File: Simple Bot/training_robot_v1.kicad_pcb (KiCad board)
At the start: 2 copper layers, 14 parts, among them J1 Conn_01x08_Socket, J2 Conn_01x04_Socket, J3 Conn_01x04_Socket, M1 Motor_DC, M2 Motor_DC, M3 Motor_DC, M4 Motor_DC, SW1 SW_SPDT_312

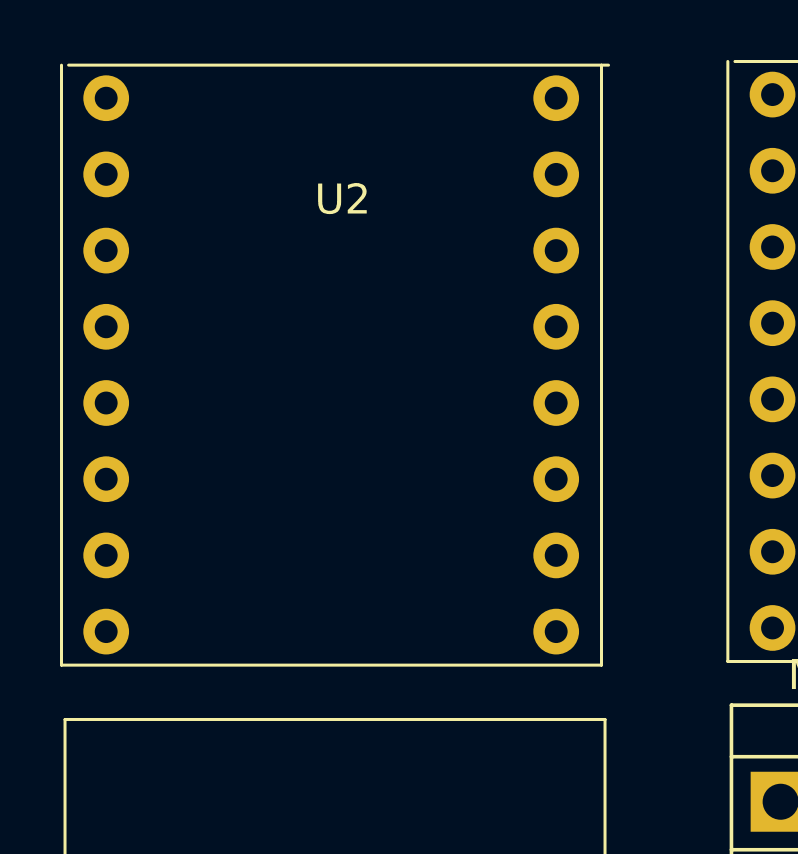
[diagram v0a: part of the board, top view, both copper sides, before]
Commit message: Removed schematic details
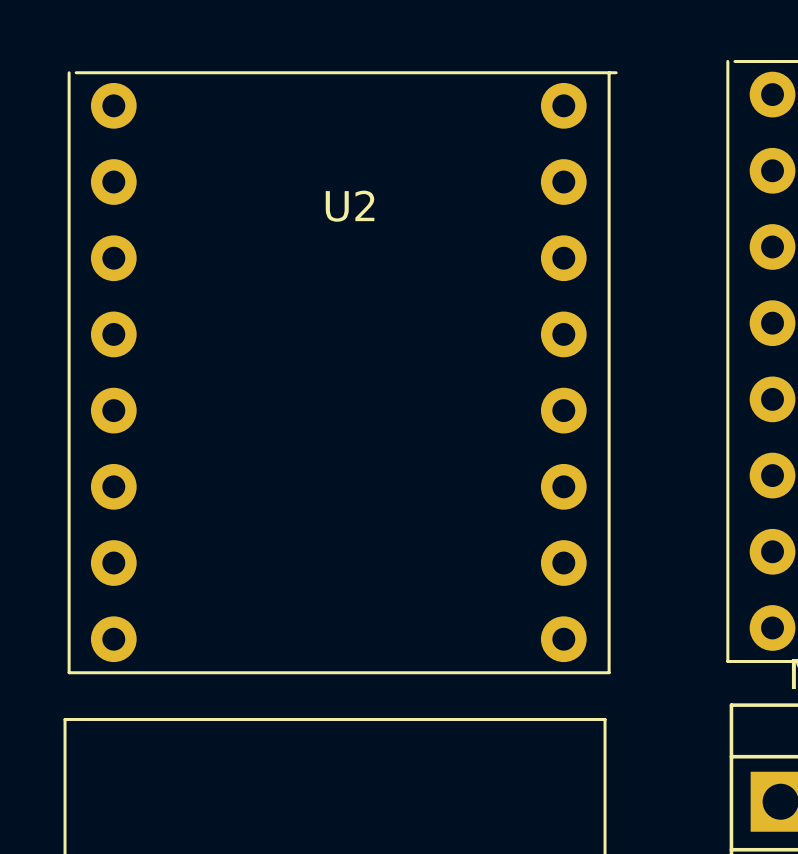
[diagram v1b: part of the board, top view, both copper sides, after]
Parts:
- moved U2 0.36 mm to (136.9, 100.1)
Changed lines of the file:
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@@
 	(footprint "custom_lib:TB_breakout_motor_driver"
 		(layer "F.Cu")
-		(at 136.644119 99.814429)
+		(at 136.898119 100.068429)
 		(property "Reference" "U2"
 			(at 0.264858 -1.698297 0)
@@
 			(polygon
 				(pts
-					(xy 127.534429 93.632) (xy 145.534429 93.632) (xy 145.534429 113.632) (xy 127.534429 113.632)
-				)
-			)
+					(xy 127.788429 93.886) (xy 145.788429 93.886) (xy 145.788429 113.886) (xy 127.788429 113.886)
+				)
+			)

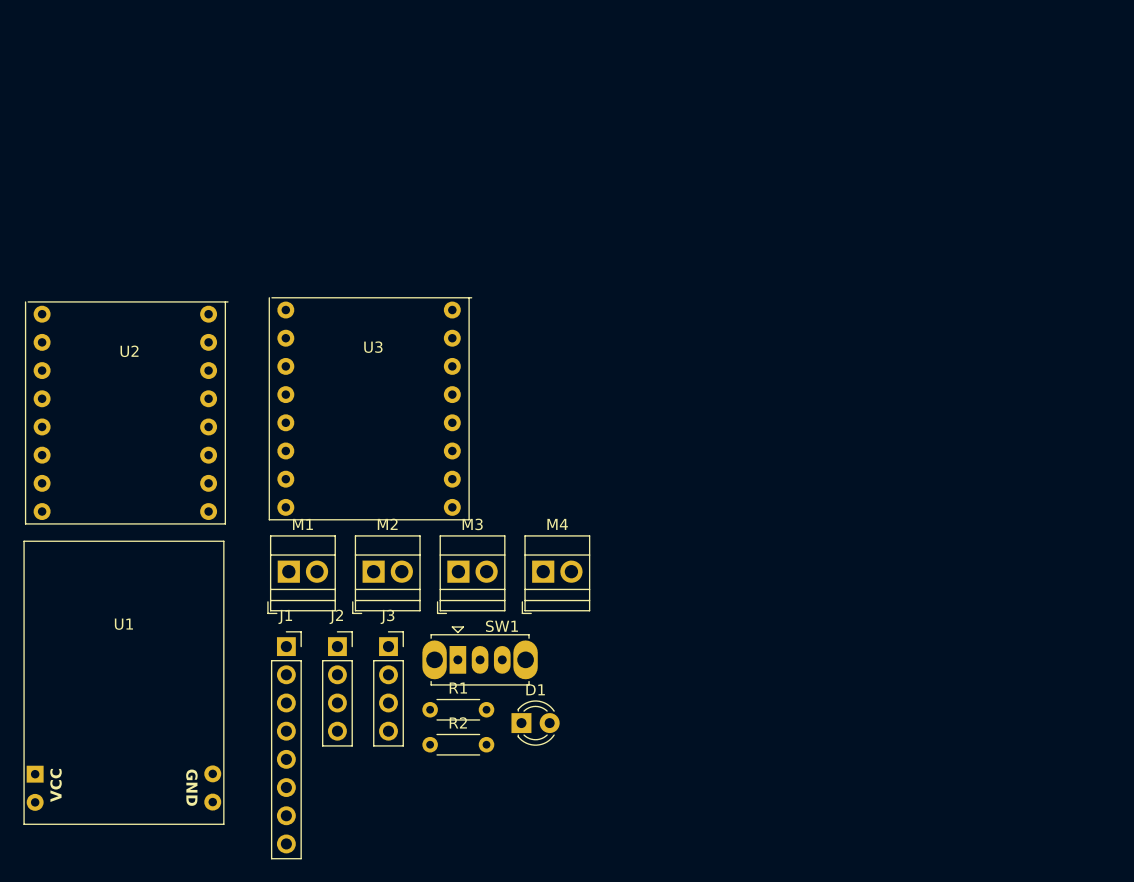
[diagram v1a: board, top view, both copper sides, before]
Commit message: replaced "simple" sch and pcb files with Josalin's
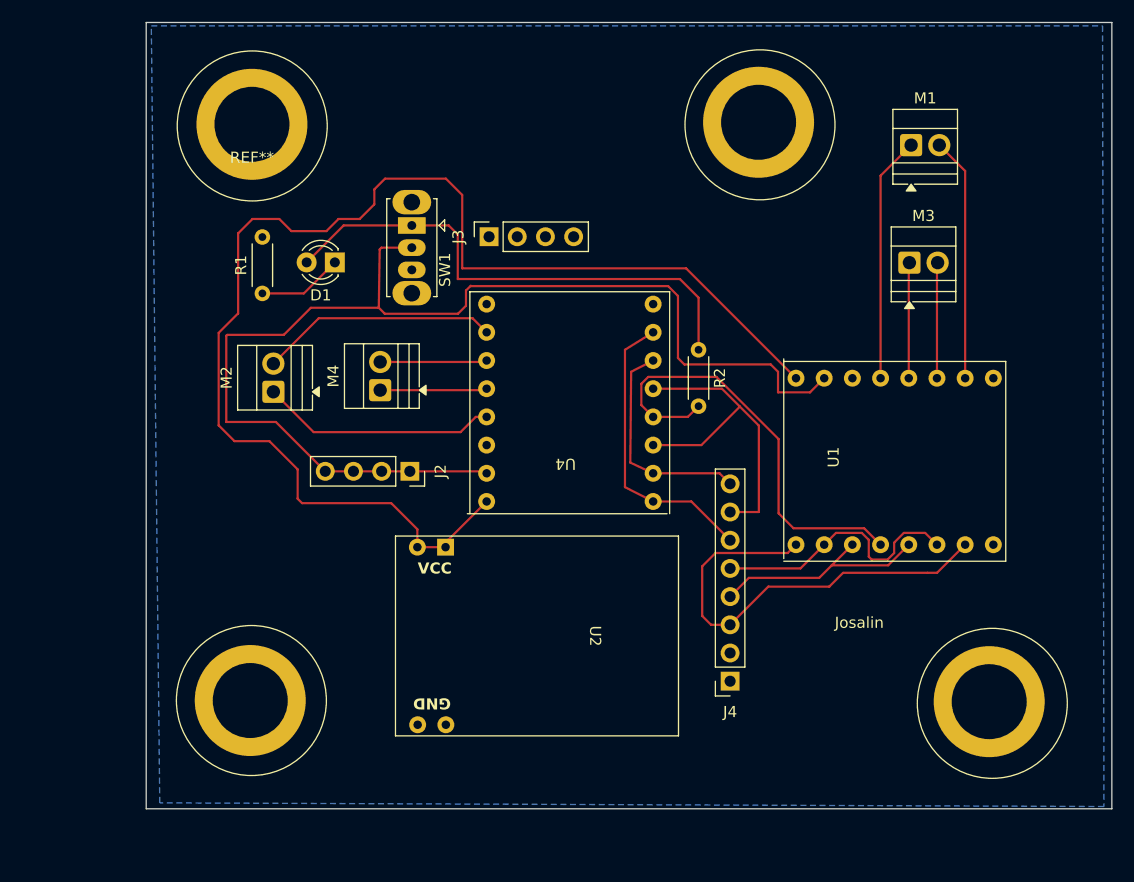
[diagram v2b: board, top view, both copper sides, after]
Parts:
- removed J1: Conn_01x08_Socket, Connector_PinSocket_2.54mm:PinSocket_1x08_P2.54mm_Vertical
- removed U3: ~, custom_lib:TB_breakout_motor_driver
- added ?: , , F.Cu at (214.6, 129.9)
- added ?: , , F.Cu at (193.8, 77.7)
- added ?: , , F.Cu at (148.0, 129.8)
- added J4: Conn_01x08_Socket, Connector_PinSocket_2.54mm:PinSocket_1x08_P2.54mm_Vertical, F.Cu at (191.3, 128.1)
- added REF**: mounting holes, training-bot-footprint:Untitled, F.Cu at (148.2, 81.4)
- added U4: R MOTOR DRIVER, training-bot-footprint:TB_breakout_motor_driver, F.Cu at (176.7, 106.8)
- R1, R2: value 10k -> R
- U1: value ~ -> L MOTOR DRIVER; footprint custom_lib:PD Module -> training-bot-footprint:TB_breakout_motor_driver
- U2: value ~ -> PD module; footprint custom_lib:TB_breakout_motor_driver -> training-bot-footprint:PD Module
- moved M1 68.0 mm to (207.6, 79.8)
- moved U1 67.4 mm to (202.3, 108.1), turned to 90 degrees
- moved M3 49.3 mm to (207.4, 90.3)
- moved U2 48.1 mm to (178.6, 124.0), turned to -90 degrees
- moved D1 44.8 mm to (155.7, 90.3), turned to 180 degrees
- moved R2 43.0 mm to (188.4, 98.2), turned to -90 degrees
- moved R1 40.4 mm to (149.1, 93.1), turned to 90 degrees
- moved SW1 39.4 mm to (162.6, 87.0), turned to -90 degrees
- moved J3 38.0 mm to (169.5, 88.0), turned to 90 degrees
- moved M4 22.0 mm to (159.7, 101.8), turned to 90 degrees
- moved M2 18.6 mm to (150.1, 102.0), turned to 90 degrees
- moved J2 17.1 mm to (162.4, 109.1), turned to -90 degrees
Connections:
- J2 pad 1: +3.3V -> VCC
- J2 pad 2: +3.3V -> VCC
- J2 pad 3: +3.3V -> VCC
- J2 pad 4: +3.3V -> VCC
- R1 pad 1: Net-(D1-A) -> Net-(D1-K)
- R1 pad 2: /STBY -> GND
- R2 pad 1: GND -> Net-(D1-A)
- R2 pad 2: Net-(D1-K) -> /STBY
- SW1 pad 2: +3.3V -> VCC
- U1 pad 1: +12V -> Net-(J4-Pin_3)
- U1 pad 2: GND -> Net-(J4-Pin_5)
- U1 pad 3: +12V -> Net-(J4-Pin_4)
- U1 pad 4: GND -> /STBY
- U2 pad 2: +3.3V -> +12V
- U2 pad 4: /FR+ -> GND
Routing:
- net +12V: track 0.00 -> 116.5 mm
- net VCC: track 0.00 -> 107.2 mm
- net Net-(D1-A): track 0.00 -> 46.4 mm
- net Net-(J4-Pin_3): track 0.00 -> 40.7 mm
- net /STBY: track 0.00 -> 39.9 mm
- net Net-(J4-Pin_7): track 0.00 -> 30.5 mm
- net Net-(J4-Pin_6): track 0.00 -> 26.6 mm
- net Net-(J4-Pin_5): track 0.00 -> 23.8 mm
- net /FL+: track 0.00 -> 22.1 mm
- net /FL-: track 0.00 -> 22.0 mm
- net /FR-: track 0.00 -> 21.4 mm
- net /FR+: track 0.00 -> 21.3 mm
- net Net-(J4-Pin_4): track 0.00 -> 20.7 mm
- net Net-(J4-Pin_8): track 0.00 -> 20.0 mm
- net /BL+: track 0.00 -> 10.4 mm
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- added copper zone on B.Cu, net GND
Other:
- board outline added: 87 x 70.8 mm
- board text added: "Josalin"
